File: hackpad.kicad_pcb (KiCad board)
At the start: 2 copper layers, 19 x 49.5 mm, 4 parts, among them SW1 SW_Push, SW2 SW_Push, SW3 SW_Push, U1 MOUDLE-SEEEDUINO-XIAO

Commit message: fixed the schematics
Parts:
- added D1: 1N914, Diode_THT:D_DO-35_SOD27_P7.62mm_Horizontal, F.Cu at (96.7, 76.5)
- added D2: SK6812MINI-E, LED_SMD:LED_SK6812MINI-E_3.2x2.8mm_P1.5mm_ReverseMount, F.Cu at (179.2, 59.5)
- added D22: 1N914, Diode_THT:D_DO-35_SOD27_P7.62mm_Horizontal, F.Cu at (96.7, 94.2)
- added D3: 1N914, Diode_THT:D_DO-35_SOD27_P7.62mm_Horizontal, F.Cu at (96.7, 80.0)
- added D5: 1N914, Diode_THT:D_DO-35_SOD27_P7.62mm_Horizontal, F.Cu at (96.7, 83.5)
- added D6: 1N914, Diode_THT:D_DO-35_SOD27_P7.62mm_Horizontal, F.Cu at (96.7, 87.1)
- added D7: 1N914, Diode_THT:D_DO-35_SOD27_P7.62mm_Horizontal, F.Cu at (96.7, 90.7)
- added D8: SK6812MINI-E, LED_SMD:LED_SK6812MINI-E_3.2x2.8mm_P1.5mm_ReverseMount, F.Cu at (179.2, 64.4)
- added D9: SK6812MINI-E, LED_SMD:LED_SK6812MINI-E_3.2x2.8mm_P1.5mm_ReverseMount, F.Cu at (179.2, 69.2)
- added D99: 1N914, Diode_THT:D_DO-35_SOD27_P7.62mm_Horizontal, F.Cu at (96.7, 97.8)
- added J1: Conn_01x04, Connector_PinHeader_2.54mm:PinHeader_1x04_P2.54mm_Vertical, F.Cu at (108.5, 53.9)
- added SW4: RotaryEncoder_Switch, Rotary_Encoder:RotaryEncoder_Alps_EC11E-Switch_Vertical_H20mm, F.Cu at (140.8, 54.0)
- added SW5: SW_Push_45deg, Button_Switch_Keyboard:SW_Cherry_MX_1.00u_PCB, F.Cu at (142.5, 88.9)
- added SW6: SW_Push_45deg, Button_Switch_Keyboard:SW_Cherry_MX_1.00u_PCB, F.Cu at (161.5, 69.9)
- added SW9: SW_Push_45deg, Button_Switch_Keyboard:SW_Cherry_MX_1.00u_PCB, F.Cu at (161.5, 88.9)
- SW1, SW2, SW3: value SW_Push -> SW_Push_45deg; moved to F.Cu
- U1: moved to F.Cu
- moved U1 78.5 mm to (93.5, 58.5), turned to 90 degrees
- moved SW3 54.6 mm to (142.5, 69.9), turned to 0 degrees
- moved SW1 41.3 mm to (123.5, 69.9), turned to 0 degrees
- moved SW2 39.2 mm to (123.5, 88.9), turned to 0 degrees
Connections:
- SW1 pad 1: Net-(U1-PA6_A10_D10_MOSI) -> Column 1
- SW1 pad 2: GND -> Net-(D99-A)
- SW2 pad 1: Net-(U1-PA5_A9_D9_MISO) -> Column 1
- SW2 pad 2: GND -> Net-(D1-A)
- SW3 pad 1: Net-(U1-PA7_A8_D8_SCK) -> Column 2
- SW3 pad 2: GND -> Net-(D5-A)
- U1 pad 1: unconnected-(U1-PA02_A0_D0-Pad1) -> Column 1
- U1 pad 10: Net-(U1-PA5_A9_D9_MISO) -> Row 2
- U1 pad 11: Net-(U1-PA6_A10_D10_MOSI) -> LEDPIN
- U1 pad 14: unconnected-(U1-5V-Pad14) -> VCC
- U1 pad 2: unconnected-(U1-PA4_A1_D1-Pad2) -> Column 2
- U1 pad 3: unconnected-(U1-PA10_A2_D2-Pad3) -> Column 3
- U1 pad 4: unconnected-(U1-PA11_A3_D3-Pad4) -> Column 4
- U1 pad 5: unconnected-(U1-PA8_A4_D4_SDA-Pad5) -> SDA
- U1 pad 6: unconnected-(U1-PA9_A5_D5_SCL-Pad6) -> SCL
- U1 pad 7: unconnected-(U1-PB08_A6_D6_TX-Pad7) -> Row 1
- U1 pad 8: unconnected-(U1-PB09_A7_D7_RX-Pad8) -> EC11B
- U1 pad 9: Net-(U1-PA7_A8_D8_SCK) -> EC11A
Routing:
- net GND: track 30.2 -> 0.00 mm
- net Net-(U1-PA7_A8_D8_SCK): track 20.6 -> 0.00 mm
- net Net-(U1-PA6_A10_D10_MOSI): track 10.1 -> 0.00 mm
- net Net-(U1-PA5_A9_D9_MISO): track 8.08 -> 0.00 mm
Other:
- board size 19 x 49.5 mm -> 3.6 x 3.2 mm

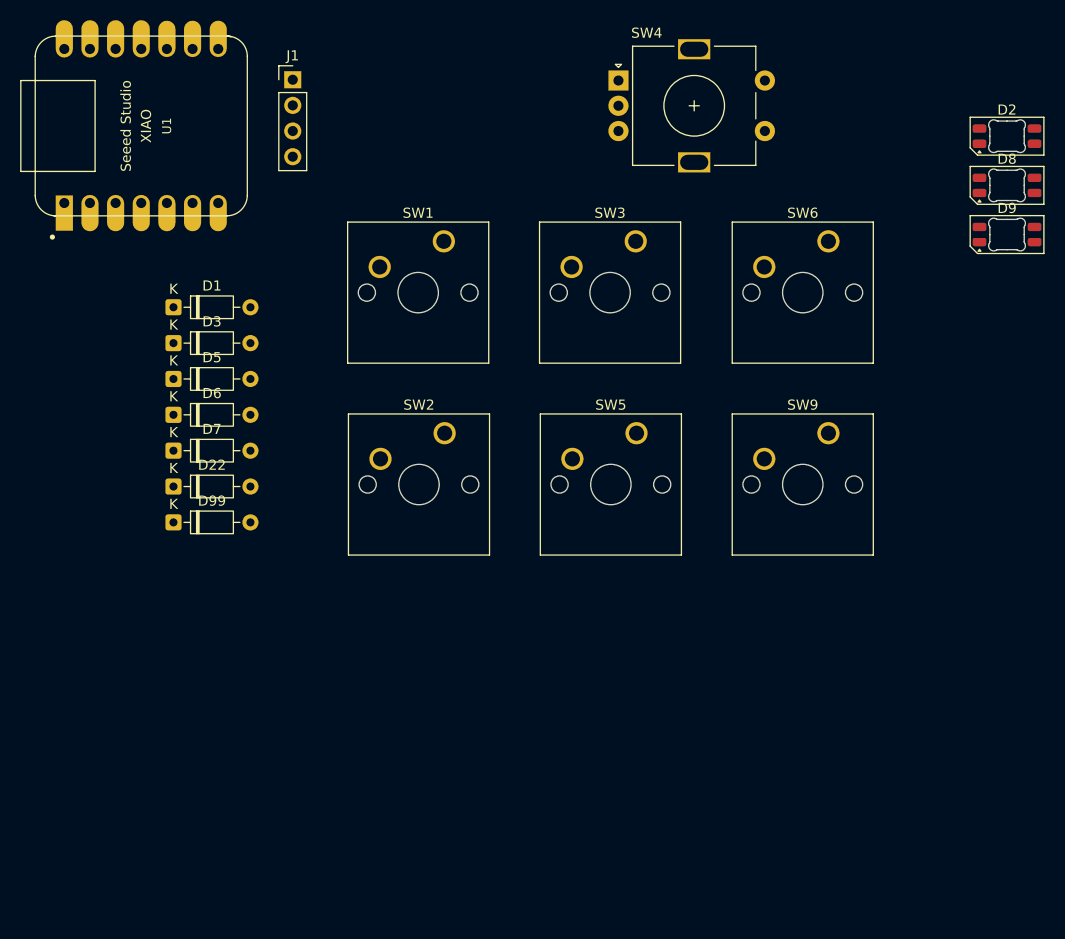
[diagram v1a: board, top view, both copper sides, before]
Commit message: Completed the pcb and added 2 extra leds in the schematic !
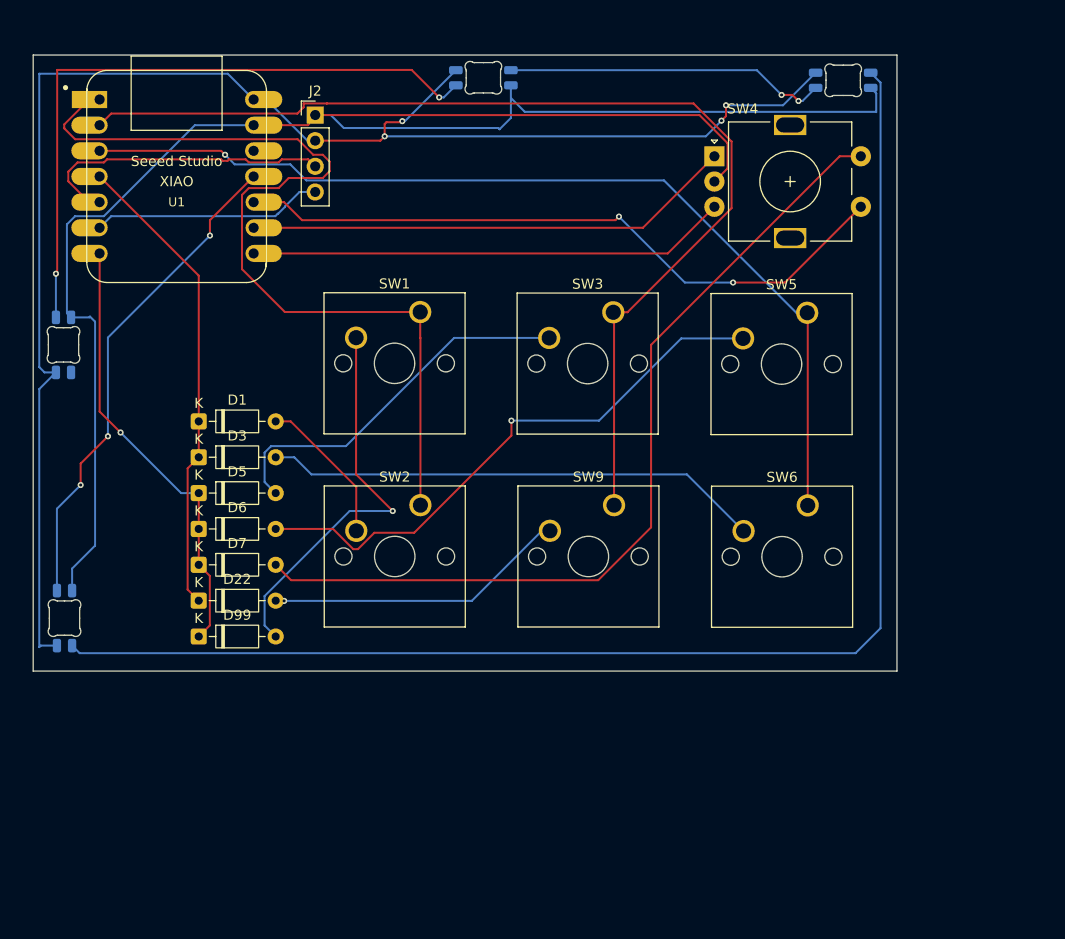
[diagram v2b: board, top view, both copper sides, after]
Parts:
- removed J1: Conn_01x04, Connector_PinHeader_2.54mm:PinHeader_1x04_P2.54mm_Vertical
- added D10: SK6812MINI-E, LED_SMD:LED_SK6812MINI-E_3.2x2.8mm_P1.5mm_ReverseMount, B.Cu at (127.4, 53.7)
- added J2: Conn_01x04_Pin, Connector_PinHeader_2.54mm:PinHeader_1x04_P2.54mm_Vertical, F.Cu at (110.7, 57.4)
- D2, D8, D9: moved to B.Cu
- moved D8 102.7 mm to (85.9, 107.2), turned to -90 degrees
- moved D2 95.7 mm to (85.8, 80.2), turned to -90 degrees
- moved SW6 26.2 mm to (159.5, 96.1)
- moved SW9 22.4 mm to (140.3, 96.0)
- moved D9 22.3 mm to (163.0, 54.0), turned to 180 degrees
- moved SW5 20.7 mm to (159.4, 77.0)
- moved SW4 12.1 mm to (150.2, 61.5)
- moved D6 11.6 mm to (99.2, 98.4)
- moved D1 11.6 mm to (99.2, 87.8)
- moved D22 11.6 mm to (99.2, 105.5)
- moved D3 11.6 mm to (99.2, 91.3)
- moved D5 11.6 mm to (99.2, 94.8)
- moved D7 11.6 mm to (99.2, 102.0)
- moved D99 11.6 mm to (99.2, 109.0)
- moved SW2 7.52 mm to (121.1, 96.0)
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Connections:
- D2 pad 2: Net-(D2-DIN) -> Net-(D10-DOUT)
- D9 pad 4: Net-(D2-DIN) -> Net-(D10-DIN)
- SW4 pad S1:  Column 4 -> EC11SWB
- U1 pad 10: Row 2 -> EC11SWB
- U1 pad 4: Column 4 -> Row 2
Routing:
- net GND: track 0.00 -> 178.0 mm
- net VCC: track 0.00 -> 154.1 mm, vias 0 -> 4
- net Net-(D8-DOUT): track 0.00 -> 136.8 mm
- net Column 2: track 0.00 -> 107.0 mm
- net Column 3: track 0.00 -> 95.8 mm, vias 0 -> 1
- net Column 1: track 0.00 -> 89.0 mm
- net EC11SWA: track 0.00 -> 86.5 mm
- net EC11SWB: track 0.00 -> 66.8 mm, vias 0 -> 2
- net Net-(D10-DOUT): track 0.00 -> 65.6 mm, vias 0 -> 2
- net Net-(D6-A): track 0.00 -> 56.6 mm, vias 0 -> 1
- net Net-(D3-A): track 0.00 -> 49.4 mm
- net LEDPIN: track 0.00 -> 49.1 mm, vias 0 -> 3
- net EC11A: track 0.00 -> 48.6 mm
- net EC11B: track 0.00 -> 47.5 mm
- net Row 2: track 0.00 -> 47.0 mm
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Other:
- board size 3.6 x 3.2 mm -> 85.5 x 61 mm
